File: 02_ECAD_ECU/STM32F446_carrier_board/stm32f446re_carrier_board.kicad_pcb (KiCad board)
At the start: 2 copper layers, 3 parts, among them J1 FX10A-168S-SV, J2 FX10A-168P-SV_(71), U1 STM32F446RETx

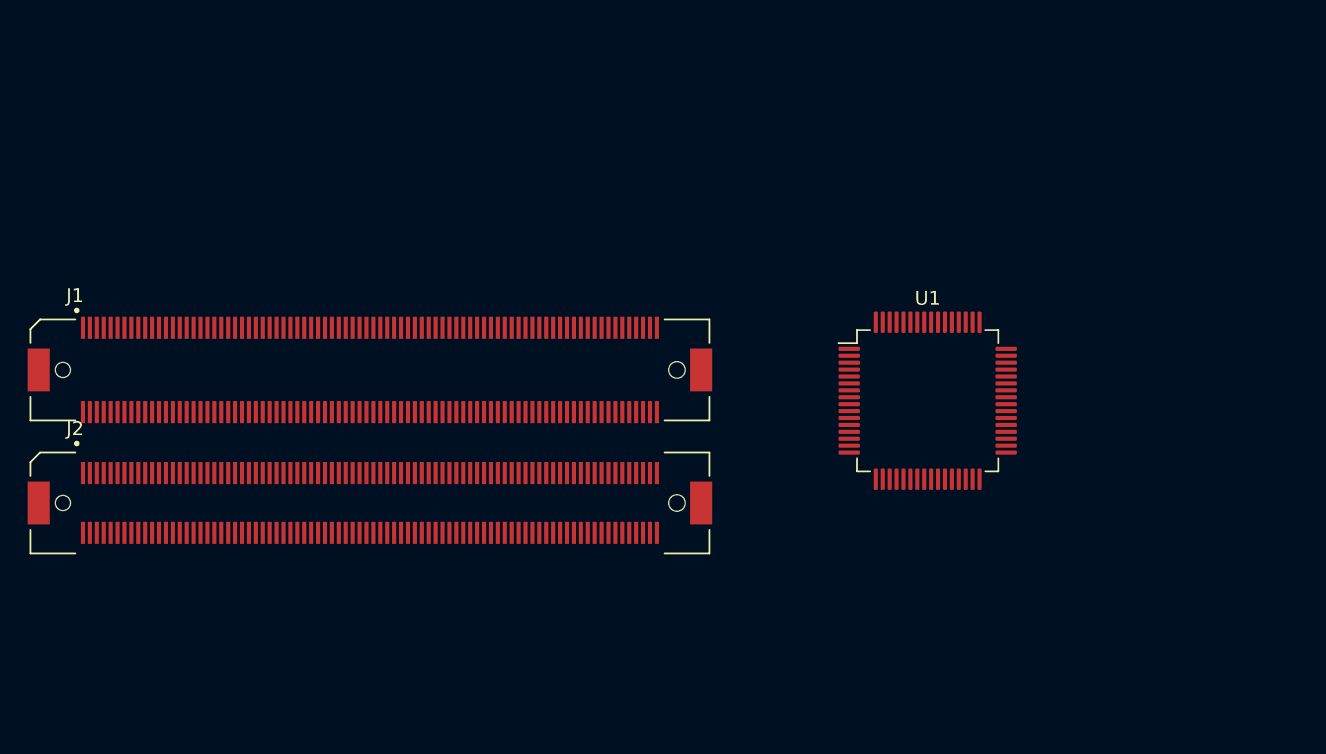
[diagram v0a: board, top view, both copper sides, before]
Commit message: added connectors to ecad project
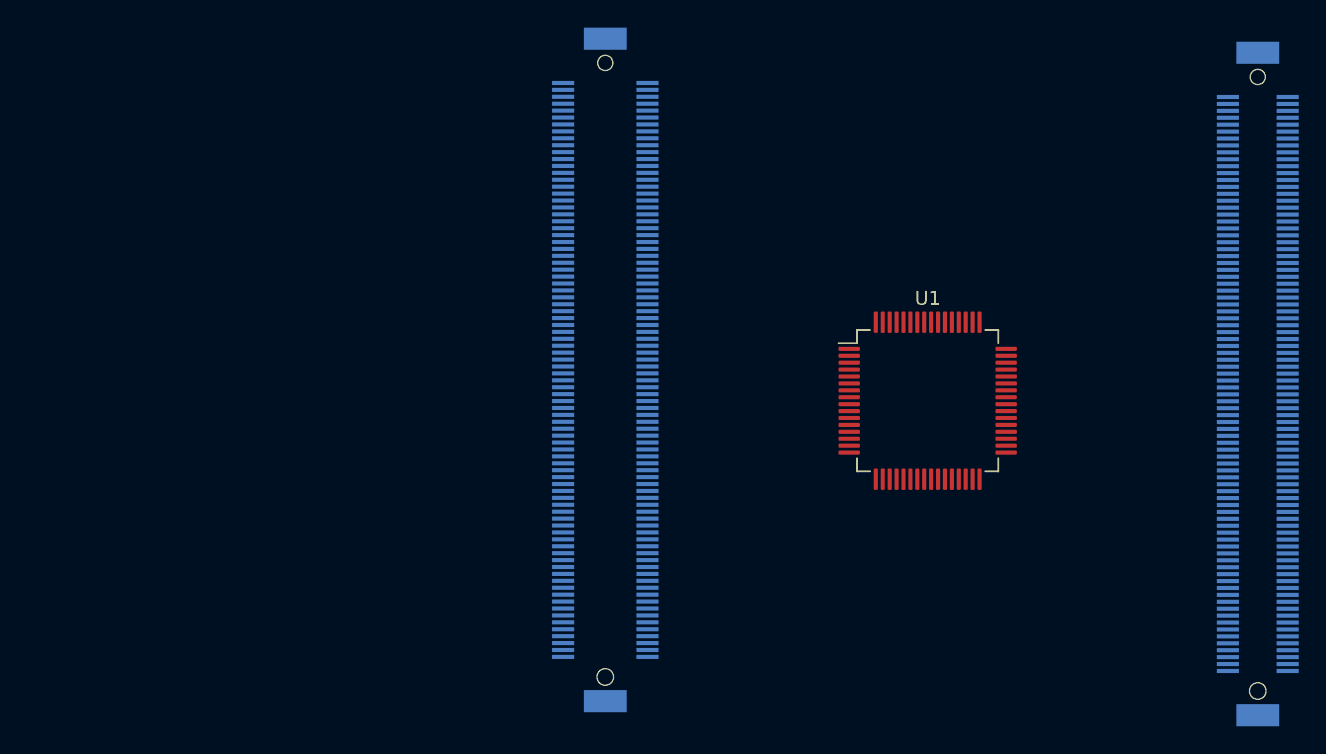
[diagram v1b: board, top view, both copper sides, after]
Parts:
- J1, J2: moved to B.Cu
- moved J2 64.8 mm to (135.4, 90.1), turned to 270 degrees
- moved J1 17.0 mm to (88.2, 89.1), turned to 270 degrees
